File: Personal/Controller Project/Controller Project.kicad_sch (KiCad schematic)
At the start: 6 parts, among them SW1 SW_Push

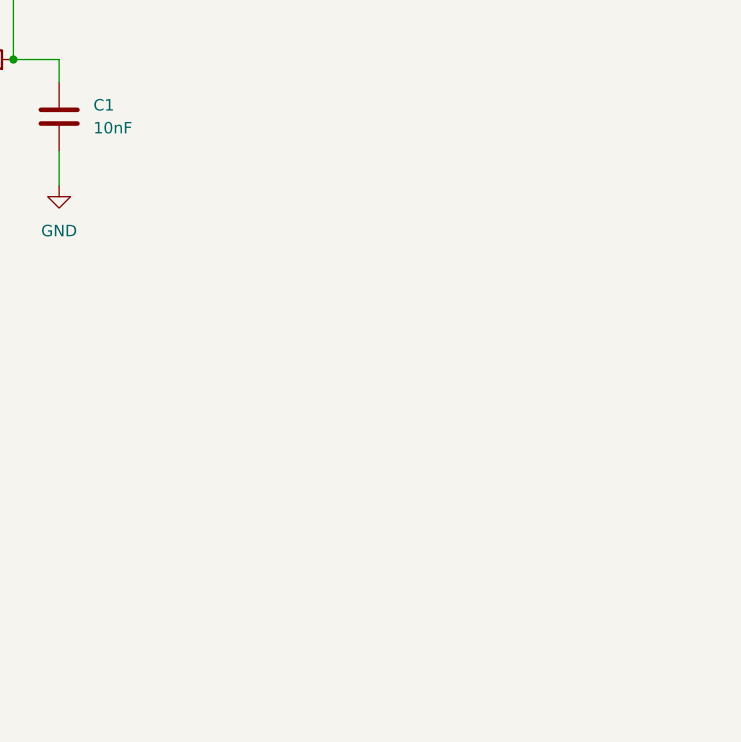
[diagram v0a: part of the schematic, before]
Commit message: ✨ Add Joystick to schematic
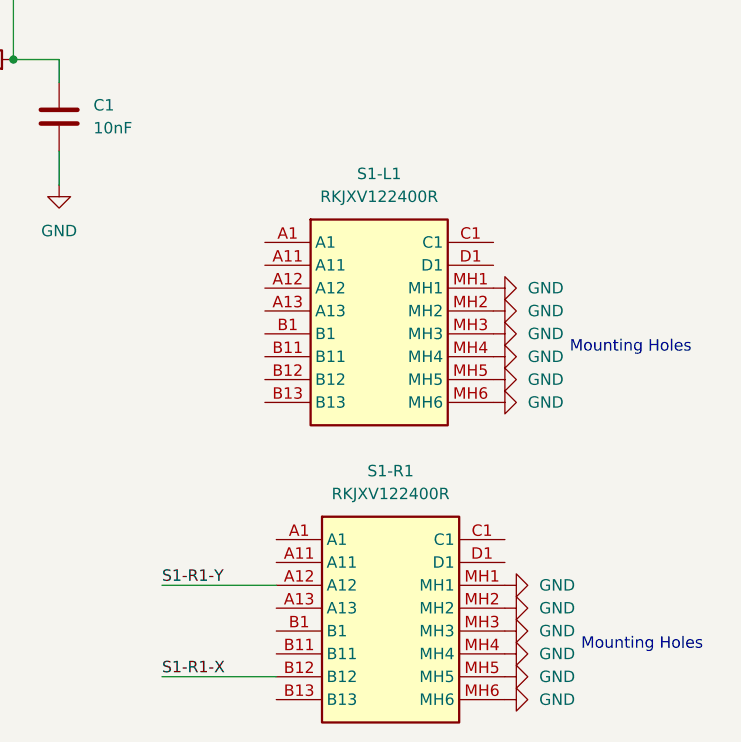
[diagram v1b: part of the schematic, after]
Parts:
- added S1-L1, S1-R1: RKJXV122400R, RKJXV122400R:RKJXV122400R, symbol RKJXV122400R:RKJXV122400R
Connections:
- net GND: now also S1-L1.MH1, S1-L1.MH2, S1-L1.MH3, S1-L1.MH4, S1-L1.MH5, S1-L1.MH6, S1-R1.MH1, S1-R1.MH2, S1-R1.MH3, S1-R1.MH4, S1-R1.MH5, S1-R1.MH6
- new net S1-R1-X: S1-R1.B12
- new net S1-R1-Y: S1-R1.A12
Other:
- note added: "Mounting Holes"

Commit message: ✨ Update schematic with new debouncing design
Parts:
- removed D1: D, Diode_THT:D_5W_P10.16mm_Horizontal, symbol Device:D
- removed D2: LED, LED_THT:LED_D3.0mm, symbol Device:LED
- added C2: C, symbol Device:C
- added R3, R4: 1k, symbol Device:R
- added SW2: SW_Push, symbol Switch:SW_Push
- C1: value 10nF -> C; footprint Capacitor_THT:C_Disc_D5.1mm_W3.2mm_P5.00mm -> (none)
- R1, R2: value 100 -> 1k; footprint Resistor_THT:R_Axial_DIN0207_L6.3mm_D2.5mm_P7.62mm_Horizontal -> (none)
- SW1: footprint Button_Switch_THT:SW_PUSH_6mm -> (none)
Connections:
- net SW_DPAD_UP is gone; now on net GND: SW1.1
- net +3.3V: no longer R1.1
- net GND: now also C2.2, SW2.1
- net BTN_RB: now reaches C1.1, R2.2
- new net: R3.2, R4.1, SW2.2
- new net +3V3: R1.1, R3.1
- new net BTN_LB: C2.1, R4.2

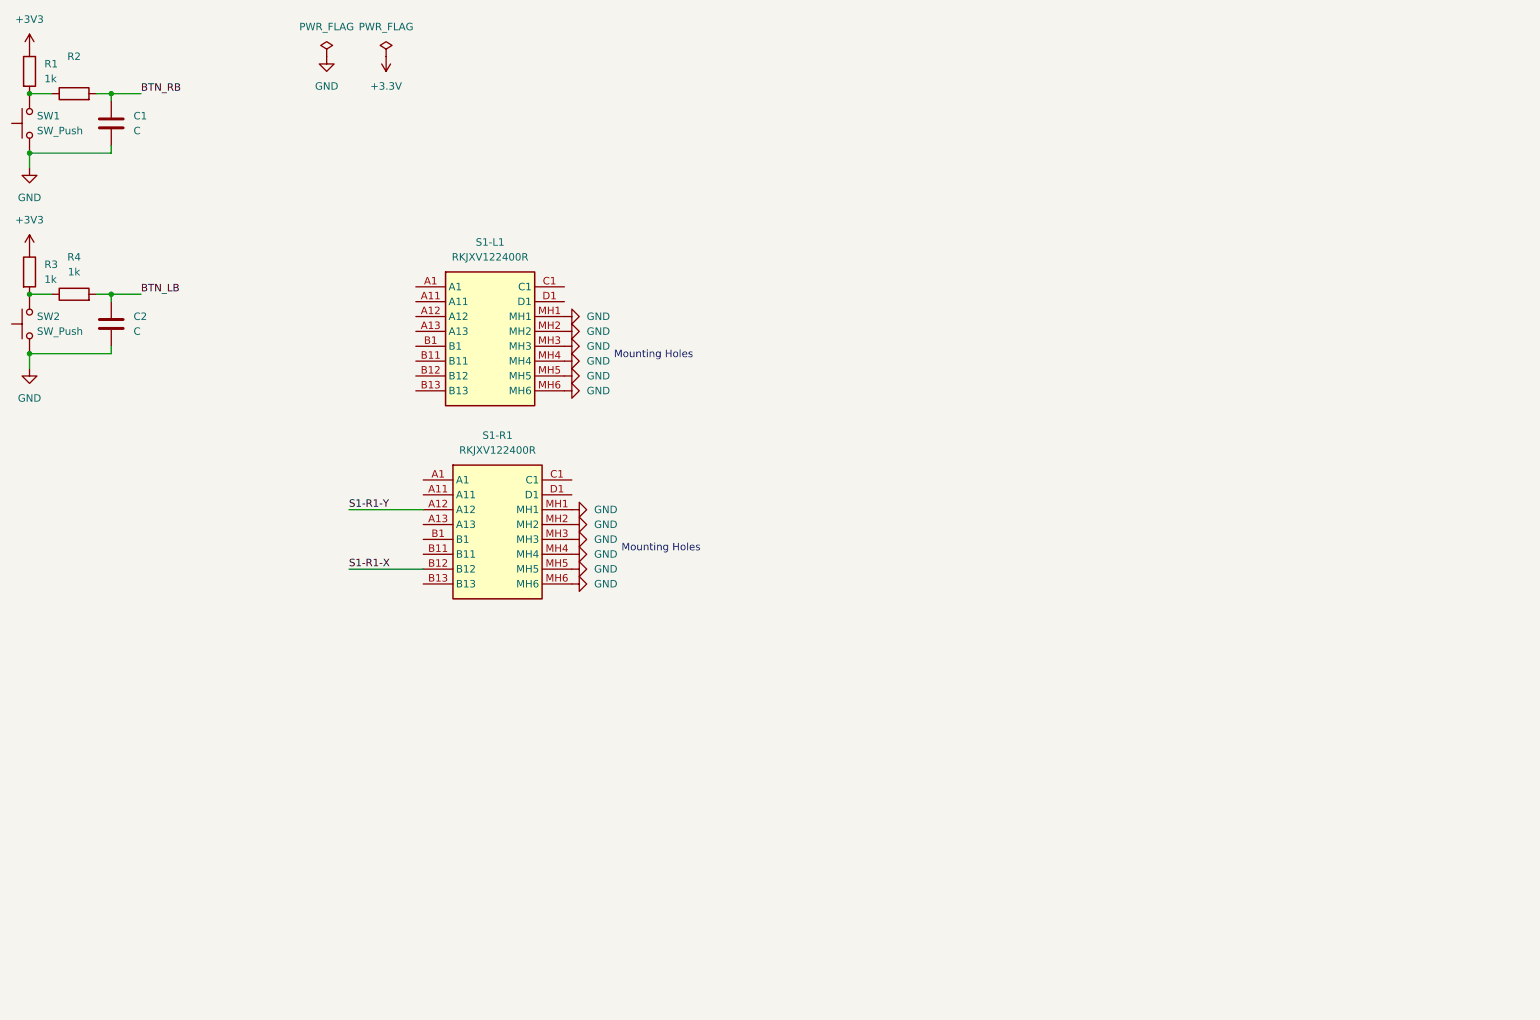
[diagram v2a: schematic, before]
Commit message: 🍱 Update schematic with most of the parts
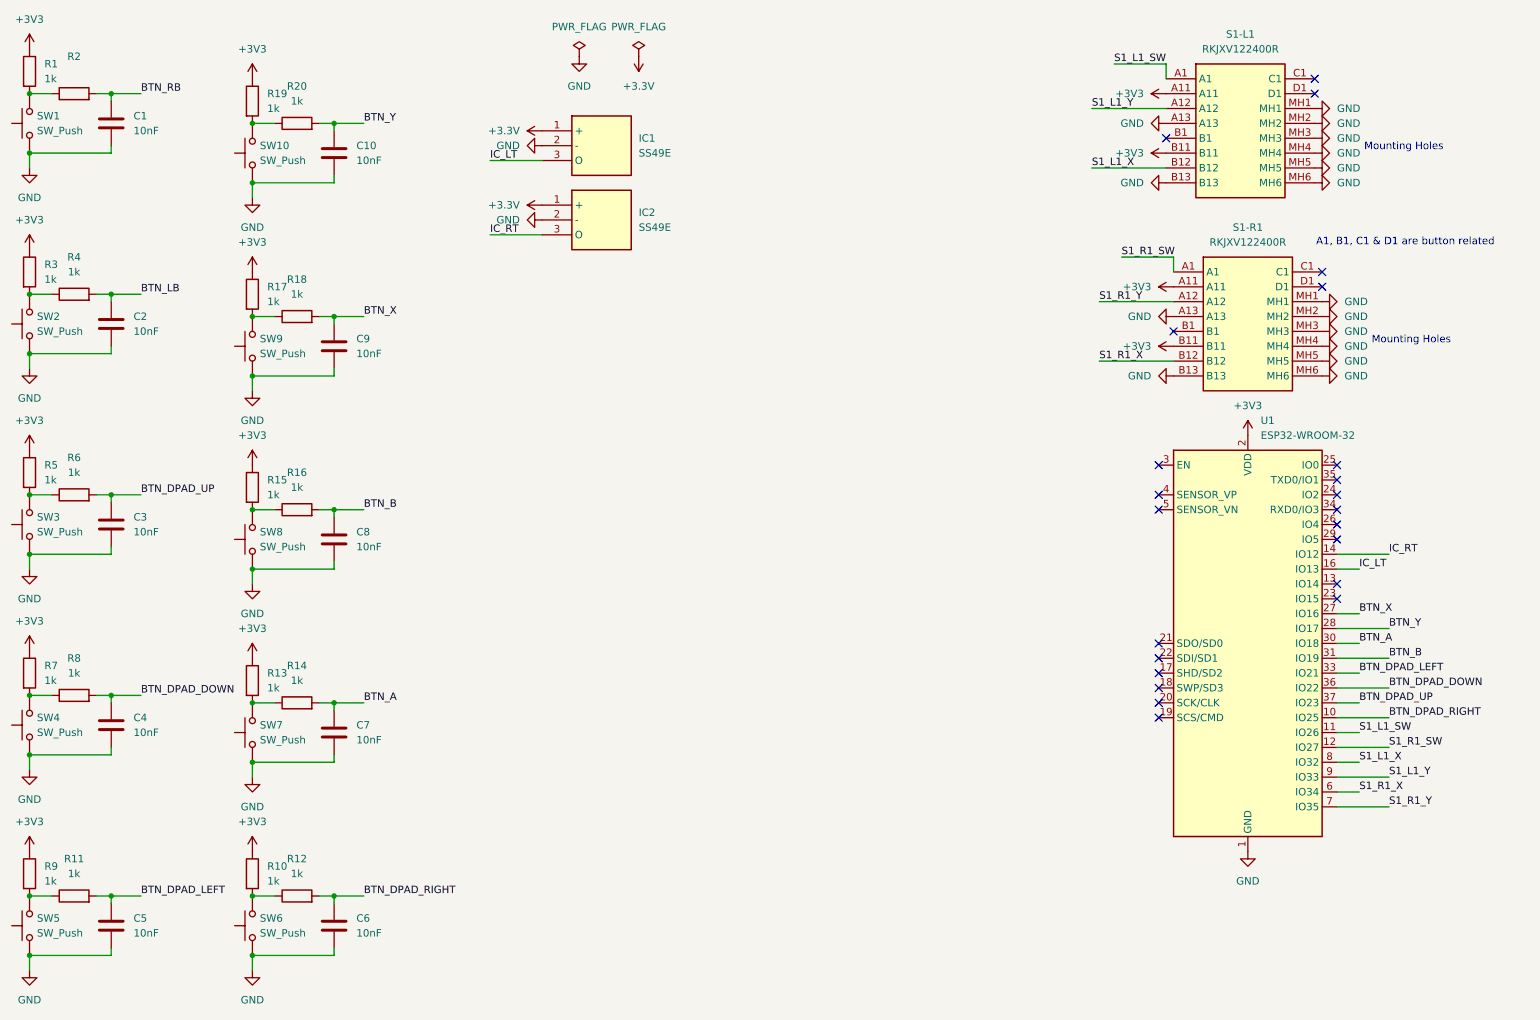
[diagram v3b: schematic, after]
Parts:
- added C10, C3, C4, C5, C6, C7, C8, C9: 10nF, symbol Device:C
- added IC1, IC2: SS49E, TO130P160X410X300-3P, symbol SS49E:SS49E
- added R10, R11, R12, R13, R14, R15, R16, R17, R18, R19, R20, R5, R6, R7, R8, R9: 1k, symbol Device:R
- added SW10, SW3, SW4, SW5, SW6, SW7, SW8, SW9: SW_Push, symbol Switch:SW_Push
- added U1: ESP32-WROOM-32, RF_Module:ESP32-WROOM-32, symbol RF_Module:ESP32-WROOM-32
- C1, C2: value C -> 10nF
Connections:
- net +3.3V: now also IC1.1 (+), IC2.1 (+)
- net +3V3: now also S1-L1.A11, S1-L1.B11, S1-R1.A11, S1-R1.B11, R10.1, R13.1, R15.1, R17.1, R19.1, R5.1, R7.1, R9.1, U1.2 (VDD)
- net GND: now also S1-L1.A13, S1-L1.B13, S1-R1.A13, S1-R1.B13, C10.2, C3.2, C4.2, C5.2, C6.2, C7.2, C8.2, C9.2, IC1.2 (-), IC2.2 (-), SW10.1, SW3.1, SW4.1, SW5.1, SW6.1, SW7.1, SW8.1, SW9.1, U1.1 (GND), U1.15 (GND), U1.38 (GND), U1.39 (GND)
- net S1_L1_SW: now reaches S1-L1.A1
- net S1_L1_SW: now also U1.11 (IO26)
- net S1_L1_Y: now reaches S1-L1.A12
- net S1_L1_Y: now also U1.9 (IO33)
- net S1_L1_X: now reaches S1-L1.B12
- net S1_L1_X: now also U1.8 (IO32)
- net S1_R1_SW: now reaches S1-R1.A1
- net S1_R1_SW: now also U1.12 (IO27)
- net S1-R1-X renamed S1_R1_X
- net S1_R1_X: now also U1.6 (IO34)
- net S1-R1-Y renamed S1_R1_Y
- net S1_R1_Y: now also U1.7 (IO35)
- new net: R11.1, R9.2, SW5.2
- new net: R17.2, R18.1, SW9.2
- new net: R19.2, R20.1, SW10.2
- new net: R5.2, R6.1, SW3.2
- new net: R15.2, R16.1, SW8.2
- new net: R13.2, R14.1, SW7.2
- new net: R10.2, R12.1, SW6.2
- new net: R7.2, R8.1, SW4.2
- new net BTN_A: C7.1, R14.2, U1.30 (IO18)
- new net BTN_B: C8.1, R16.2, U1.31 (IO19)
- new net BTN_DPAD_DOWN: C4.1, R8.2, U1.36 (IO22)
- new net BTN_DPAD_LEFT: C5.1, R11.2, U1.33 (IO21)
- new net BTN_DPAD_RIGHT: C6.1, R12.2, U1.10 (IO25)
- new net BTN_DPAD_UP: C3.1, R6.2, U1.37 (IO23)
- new net BTN_X: C9.1, R18.2, U1.27 (IO16)
- new net BTN_Y: C10.1, R20.2, U1.28 (IO17)
- new net IC_LT: IC1.3 (O), U1.16 (IO13)
- new net IC_RT: IC2.3 (O), U1.14 (IO12)
- no-connect marks 0 -> 23
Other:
- note added: "A1, B1, C1 & D1 are button related"
- company: (none) -> Nathan Thus
- title: (none) -> ESP32 Controller Project
- moved on the sheet: S1-L1, S1-R1

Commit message: 🍱 Update schematic with final parts
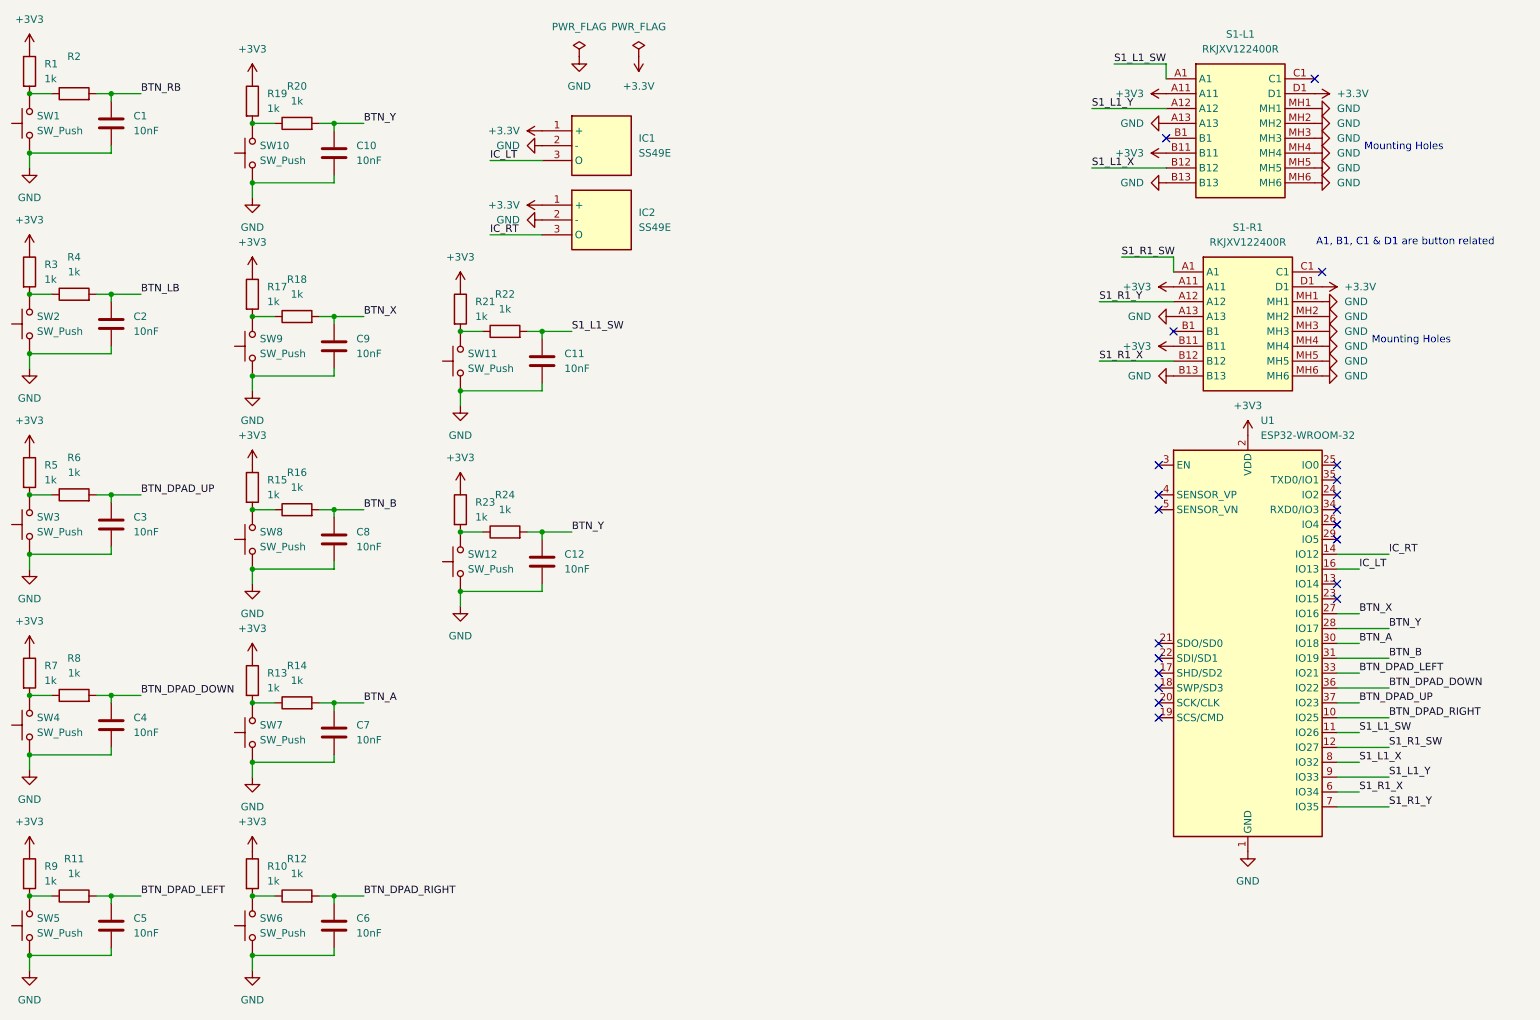
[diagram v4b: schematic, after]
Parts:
- added C11, C12: 10nF, Capacitor_THT:CP_Axial_L10.0mm_D6.0mm_P15.00mm_Horizontal, symbol Device:C
- added R21, R22, R23, R24: 1k, Resistor_THT:R_Axial_DIN0204_L3.6mm_D1.6mm_P5.08mm_Horizontal, symbol Device:R
- added SW11, SW12: SW_Push, Button_Switch_THT:SW_PUSH_6mm, symbol Switch:SW_Push
- C1, C10, C2, C3, C4, C5, C6, C7, C8, C9: footprint (none) -> Capacitor_THT:CP_Axial_L10.0mm_D6.0mm_P15.00mm_Horizontal
- R1, R10, R11, R12, R13, R14, R15, R16, R17, R18, R19, R2, R20, R3, R4, R5, R6, R7, R8, R9: footprint (none) -> Resistor_THT:R_Axial_DIN0204_L3.6mm_D1.6mm_P5.08mm_Horizontal
- S1-L1, S1-R1: footprint RKJXV122400R:RKJXV122400R -> RKJXV122400R
- SW1, SW2: footprint (none) -> Button_Switch_THT:SW_CW_GPTS203211B
- SW10, SW3, SW4, SW5, SW6, SW7, SW8, SW9: footprint (none) -> Button_Switch_THT:SW_PUSH_6mm
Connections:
- net +3.3V: now also S1-L1.D1, S1-R1.D1
- net +3V3: now also R21.1, R23.1
- net BTN_Y: now also C12.1, R24.2
- net GND: now also C11.2, C12.2, SW11.1, SW12.1
- net S1_L1_SW: now also C11.1, R22.2
- new net: R23.2, R24.1, SW12.2
- new net: R21.2, R22.1, SW11.2
- no-connect marks 23 -> 21

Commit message: 🍱 Update Trace Design for PCB
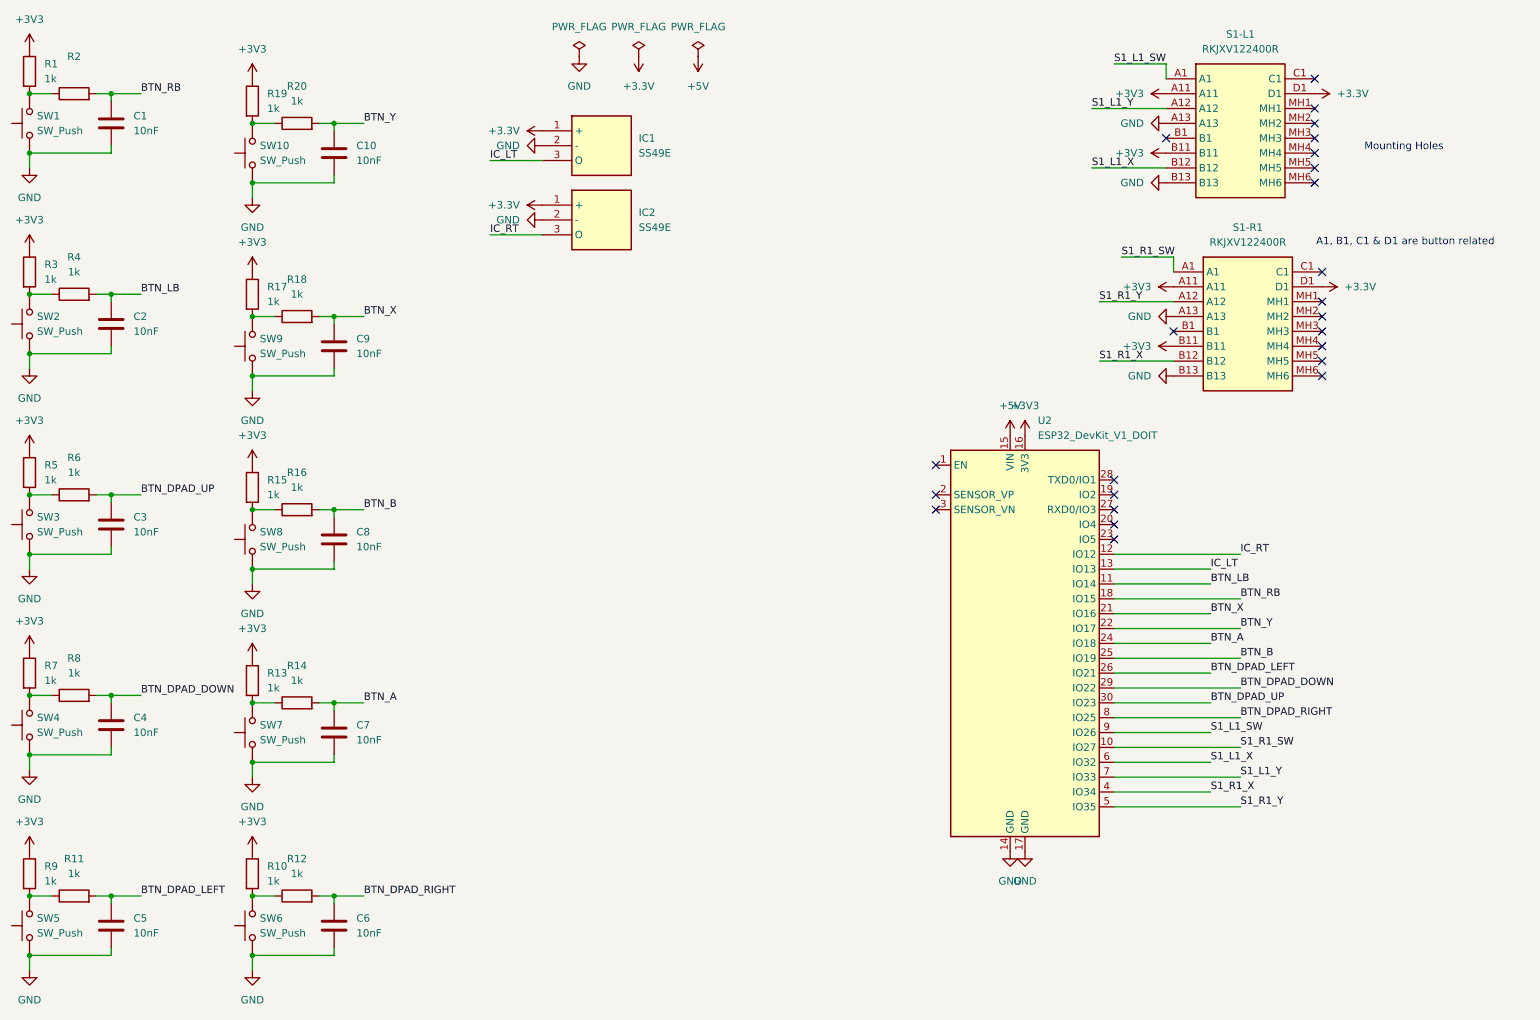
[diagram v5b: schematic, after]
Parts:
- removed C11, C12: 10nF, Capacitor_THT:CP_Axial_L10.0mm_D6.0mm_P15.00mm_Horizontal, symbol Device:C
- removed R21, R22, R23, R24: 1k, Resistor_THT:R_Axial_DIN0204_L3.6mm_D1.6mm_P5.08mm_Horizontal, symbol Device:R
- removed SW11, SW12: SW_Push, Button_Switch_THT:SW_PUSH_6mm, symbol Switch:SW_Push
- removed U1: ESP32-WROOM-32, RF_Module:ESP32-WROOM-32, symbol RF_Module:ESP32-WROOM-32
- added U2: ESP32_DevKit_V1_DOIT, ESP32_DevKit_V1_DOIT:esp32_devkit_v1_doit, symbol ESP32:ESP32_DevKit_V1_DOIT
- C1, C10, C2, C3, C4, C5, C6, C7, C8, C9: footprint Capacitor_THT:CP_Axial_L10.0mm_D6.0mm_P15.00mm_Horizontal -> Capacitor_THT:CP_Radial_D5.0mm_P2.50mm
- IC1, IC2: footprint TO130P160X410X300-3P -> SS49E:SS49E
- S1-L1, S1-R1: footprint RKJXV122400R -> RKJXV122400R:RKJXV122400R
- SW1, SW2: footprint Button_Switch_THT:SW_CW_GPTS203211B -> Button_Switch_THT:SW_PUSH_6mm
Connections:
- net +3V3: now also U2.16 (3V3)
- net BTN_A: now also U2.24 (IO18)
- net BTN_B: now also U2.25 (IO19)
- net BTN_DPAD_DOWN: now also U2.29 (IO22)
- net BTN_DPAD_LEFT: now also U2.26 (IO21)
- net BTN_DPAD_RIGHT: now also U2.8 (IO25)
- net BTN_DPAD_UP: now also U2.30 (IO23)
- net BTN_LB: now also U2.11 (IO14)
- net BTN_RB: now also U2.18 (IO15)
- net BTN_X: now also U2.21 (IO16)
- net BTN_Y: now also U2.22 (IO17)
- net GND: now also U2.14 (GND), U2.17 (GND); no longer S1-L1.MH1, S1-L1.MH2, S1-L1.MH3, S1-L1.MH4, S1-L1.MH5, S1-L1.MH6, S1-R1.MH1, S1-R1.MH2, S1-R1.MH3, S1-R1.MH4, S1-R1.MH5, S1-R1.MH6
- net IC_LT: now also U2.13 (IO13)
- net IC_RT: now also U2.12 (IO12)
- net S1_L1_SW: now also U2.9 (IO26)
- net S1_L1_X: now also U2.6 (IO32)
- net S1_L1_Y: now also U2.7 (IO33)
- net S1_R1_SW: now also U2.10 (IO27)
- net S1_R1_X: now also U2.4 (IO34)
- net S1_R1_Y: now also U2.5 (IO35)
- new net +5V: U2.15 (VIN)
- no-connect marks 21 -> 24
